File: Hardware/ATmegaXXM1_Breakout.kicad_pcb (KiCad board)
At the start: 2 copper layers, 57.1 x 50.2 mm, 37 parts, among them P1 VIN, P10 UART, P11 AREF, P12 Mounting Hole, P13 Mounting Hole, P14 Mounting Hole, P15 Mounting Hole, P2 PORTB, P3 PORTC, P4 PORTD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

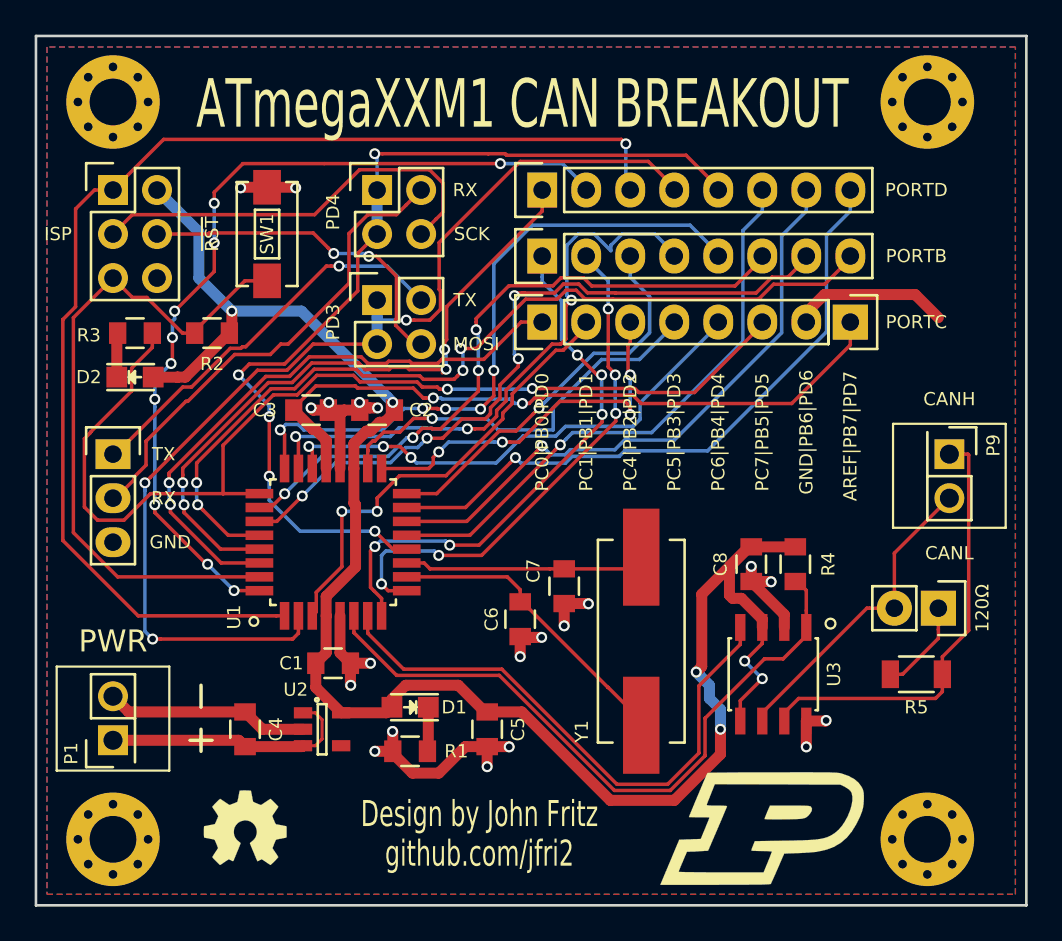
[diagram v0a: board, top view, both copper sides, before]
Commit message: Fixed gnd fill on mounting holes & added vias connecting top & bottom gnd planes
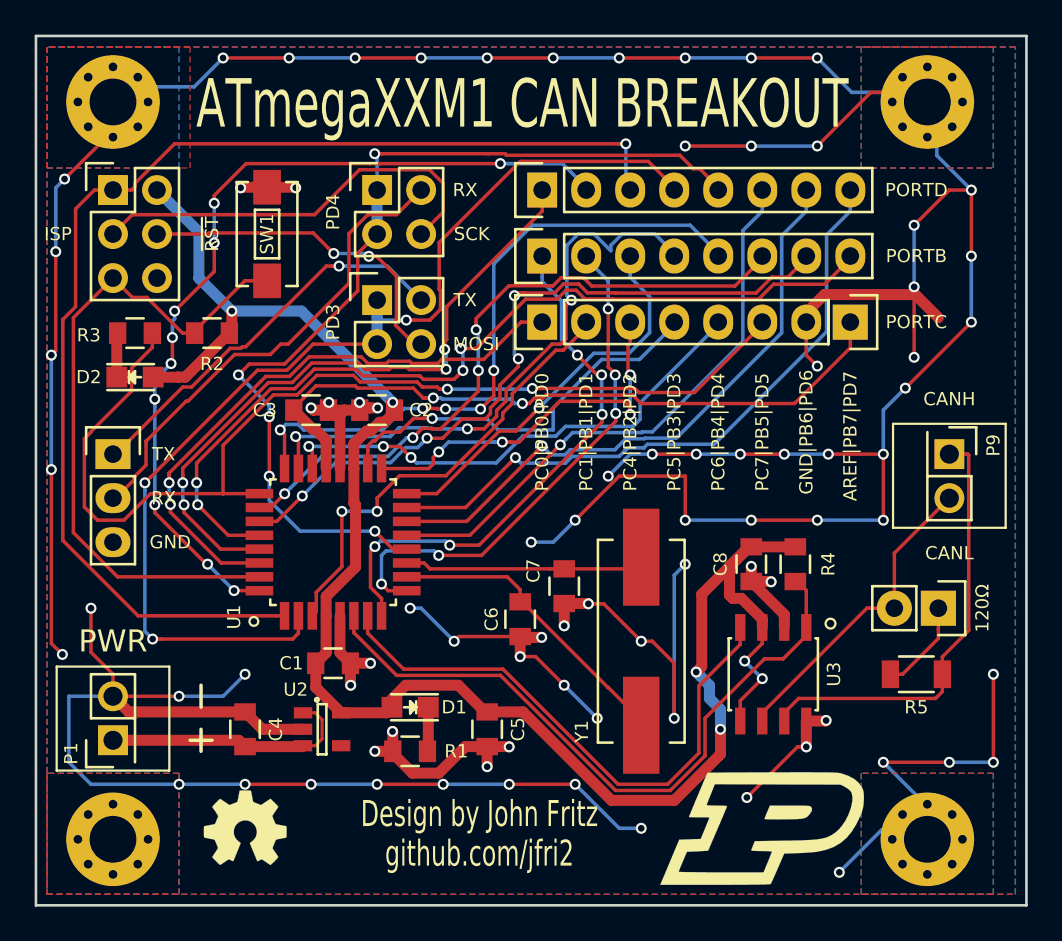
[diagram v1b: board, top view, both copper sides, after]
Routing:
- net GND: track 62.3 -> 356.9 mm, vias 20 -> 83

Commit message: Re-save of last commit
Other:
- rule pad_to_mask_clearance: 0.0762 -> 0.0635
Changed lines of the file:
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@@
     (links 89)
     (no_connects 1)
-    (area 53.899999 36.754999 111.200001 87.070001)
+    (area 52.862838 36.0126 127.535715 97.315001)
     (thickness 1.6)
     (drawings 38)
@@
     (pad_size 1.524 1.524)
     (pad_drill 0.762)
-    (pad_to_mask_clearance 0.0762)
+    (pad_to_mask_clearance 0.0635)
     (pad_to_paste_clearance -0.127)
     (aux_axis_origin 0 0)
     (visible_elements 7FFFFFFF)
     (pcbplotparams
-      (layerselection 0x0b0a8_80000001)
+      (layerselection 0x0b0e8_80000001)
       (usegerberextensions false)
       (excludeedgelayer true)

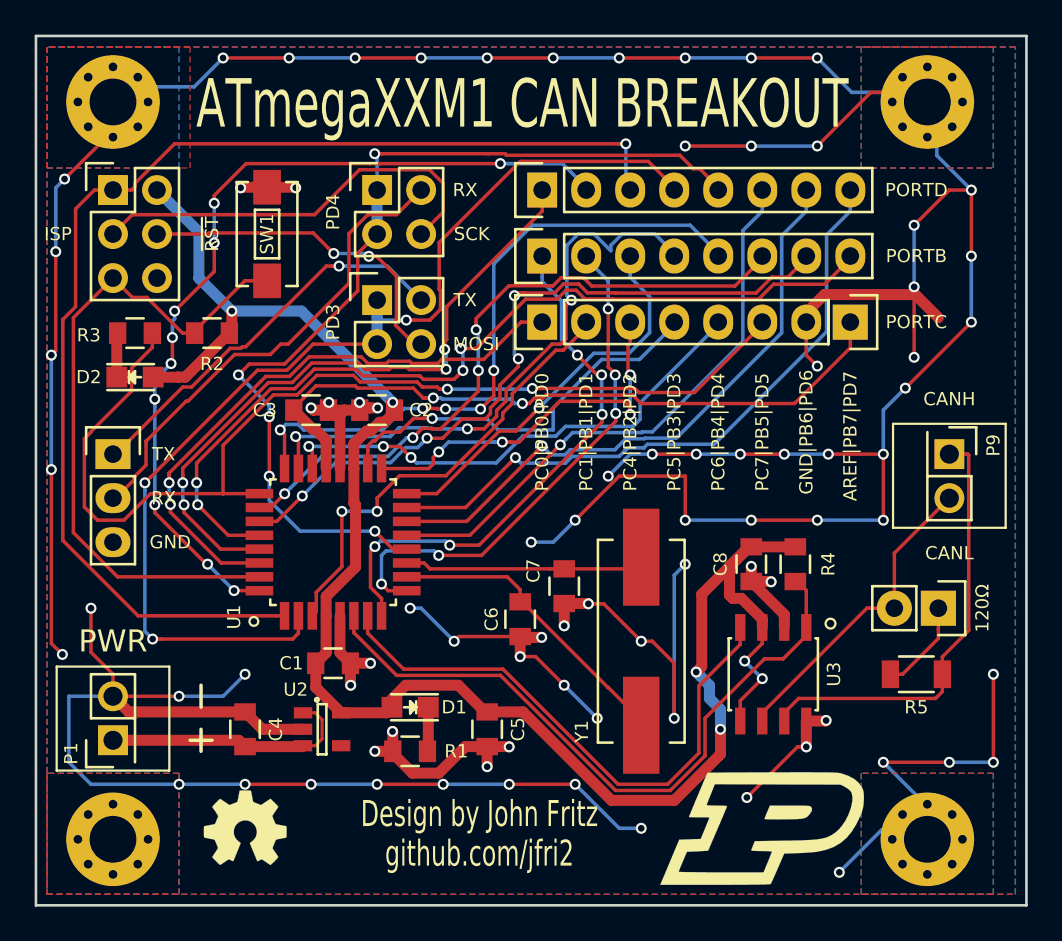
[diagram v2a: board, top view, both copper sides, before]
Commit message: Changed routing & removed via in pad. Regenerated gerbers
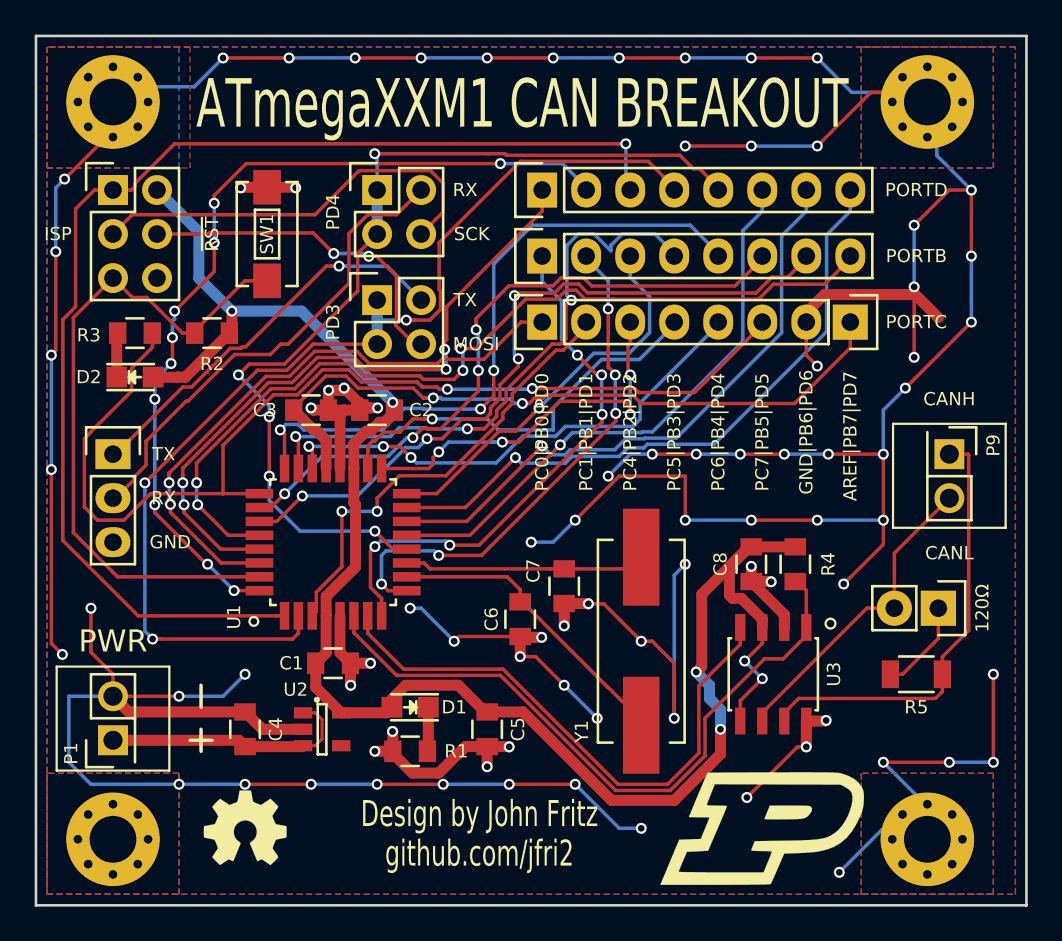
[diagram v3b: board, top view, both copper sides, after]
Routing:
- net GND: track 356.9 -> 365.3 mm, vias 83 -> 84
- net /PB4: vias 5 -> 3
